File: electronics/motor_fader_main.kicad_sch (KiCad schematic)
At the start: 29 parts, among them J1 Conn_01x04_MountingPin, J2 Program, J3 Conn_01x04_MountingPin, U1 ATtiny816-M, U2 DRV8837

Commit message: updates
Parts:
- U1: value ATtiny816-M -> ATtiny1616-M; symbol MCU_Microchip_ATtiny:ATtiny816-M -> MCU_Microchip_ATtiny:ATtiny1616-M
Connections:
- net DBG_LED: now also U1.12 (PB2); no longer U1.18 (PC3)
- net TOUCH: now also U1.18 (PC3); no longer U1.8 (PA7)
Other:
- note added: "Note: Must be ATtiny1616 or ATtiny3216 for 2 independent ADC peripherals, for simultaneous touch + potentiometer."
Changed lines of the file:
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@@
 	(wire
 		(pts
+			(xy 69.85 99.06) (xy 85.09 99.06)
+		)
+		(stroke
+			(width 0)
+			(type default)
+		)
+	)
+	(wire
+		(pts
 			(xy 69.85 86.36) (xy 85.09 86.36)
 		)
@@
 		)
 	)
+	(text "Note: Must be ATtiny1616 or ATtiny3216 for\n2 independent ADC peripherals, for\nsimultaneous touch + potentiometer."
+		(exclude_from_sim no)
+		(at 28.194 50.546 0)
+		(effects
+			(font
+				(size 1.27 1.27)
+			)
+			(justify left)
+		)
+	)
 	(label "DBG_LED"
-		(at 24.13 101.6 0)
+		(at 85.09 99.06 180)
 		(effects
 			(font
 				(size 1.27 1.27)
 			)
-			(justify left bottom)
+			(justify right bottom)
 		)
 	)
@@
 	)
 	(label "TOUCH"
-		(at 85.09 88.9 180)
+		(at 24.13 101.6 0)
 		(effects
 			(font
 				(size 1.27 1.27)
 			)
-			(justify right bottom)
+			(justify left bottom)
 		)
 	)
@@
 	)
 	(symbol
-		(lib_id "MCU_Microchip_ATtiny:ATtiny816-M")
+		(lib_id "MCU_Microchip_ATtiny:ATtiny1616-M")
 		(at 54.61 88.9 0)
 		(unit 1)
@@
 		(fields_autoplaced yes)
 		(property "Reference" "U1"
-			(at 56.6294 63.5 0)
+			(at 56.8041 63.5 0)
 			(effects
 				(font
@@
 			)
 		)
-		(property "Value" "ATtiny816-M"
-			(at 56.6294 66.04 0)
+		(property "Value" "ATtiny1616-M"
+			(at 56.8041 66.04 0)
 			(effects
 				(font
@@
 			)
 		)
-		(property "Datasheet" "http://ww1.microchip.com/downloads/en/DeviceDoc/40001913A.pdf"
+		(property "Datasheet" "http://ww1.microchip.com/downloads/en/DeviceDoc/ATtiny3216_ATtiny1616-data-sheet-40001997B.pdf"
 			(at 54.61 88.9 0)
 			(effects
@@
 			)
 		)
-		(property "Description" ""
+		(property "Description" "20MHz, 16kB Flash, 2kB SRAM, 256B EEPROM, VQFN-20"
 			(at 54.61 88.9 0)
 			(effects

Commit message: Updates
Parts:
- added TP6: PA3, modified:TestPoint_THTPad_D1.0mm_Drill0.5mm_small_valuesilk, symbol Connector:TestPoint_Small
- TP1: value P?? -> PA7
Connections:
- net at TP1.1: now also U1.8 (PA7)
- net at U1.2 (PA3): now also TP6.1
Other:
- moved on the sheet: TP1
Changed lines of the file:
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@@
 	(wire
 		(pts
+			(xy 69.85 78.74) (xy 78.74 78.74)
+		)
+		(stroke
+			(width 0)
+			(type default)
+		)
+	)
+	(wire
+		(pts
 			(xy 153.67 115.57) (xy 153.67 119.38)
 		)
@@
 	(wire
 		(pts
-			(xy 69.85 88.9) (xy 85.09 88.9)
+			(xy 76.2 176.53) (xy 77.47 176.53)
 		)
 		(stroke
@@
 	(wire
 		(pts
-			(xy 76.2 176.53) (xy 77.47 176.53)
+			(xy 166.37 139.7) (xy 184.15 139.7)
 		)
 		(stroke
@@
 	(wire
 		(pts
-			(xy 166.37 139.7) (xy 184.15 139.7)
+			(xy 73.66 166.37) (xy 77.47 166.37)
 		)
 		(stroke
@@
 	(wire
 		(pts
-			(xy 73.66 166.37) (xy 77.47 166.37)
+			(xy 140.97 66.04) (xy 146.05 66.04)
 		)
 		(stroke
@@
 	(wire
 		(pts
-			(xy 140.97 66.04) (xy 146.05 66.04)
+			(xy 219.71 133.35) (xy 229.87 133.35)
 		)
 		(stroke
@@
 	(wire
 		(pts
-			(xy 219.71 133.35) (xy 229.87 133.35)
+			(xy 71.12 171.45) (xy 71.12 186.69)
 		)
 		(stroke
@@
 	(wire
 		(pts
-			(xy 71.12 171.45) (xy 71.12 186.69)
+			(xy 69.85 76.2) (xy 85.09 76.2)
 		)
 		(stroke
@@
 	(wire
 		(pts
-			(xy 69.85 76.2) (xy 85.09 76.2)
+			(xy 69.85 88.9) (xy 78.74 88.9)
 		)
 		(stroke
@@
 	(symbol
 		(lib_id "Connector:TestPoint_Small")
-		(at 90.17 60.96 0)
+		(at 78.74 88.9 0)
 		(unit 1)
 		(exclude_from_sim no)
@@
 		(dnp no)
 		(property "Reference" "TP1"
-			(at 91.44 60.96 0)
+			(at 80.01 88.9 0)
 			(effects
 				(font
@@
 			)
 		)
-		(property "Value" "P??"
-			(at 96.52 60.96 0)
+		(property "Value" "PA7"
+			(at 85.09 88.9 0)
 			(effects
 				(font
@@
 		)
 		(property "Footprint" "modified:TestPoint_THTPad_D1.0mm_Drill0.5mm_small_valuesilk"
-			(at 95.25 60.96 0)
+			(at 83.82 88.9 0)
 			(effects
 				(font
@@
 		)
 		(property "Datasheet" "~"
-			(at 95.25 60.96 0)
+			(at 83.82 88.9 0)
 			(effects
 				(font
@@
 		)
 		(property "Description" ""
-			(at 90.17 60.96 0)
+			(at 78.74 88.9 0)
 			(effects
 				(font
@@
 					(unit 1)
 				)
+			)
+		)
+	)
+	(symbol
+		(lib_id "Connector:TestPoint_Small")
+		(at 78.74 78.74 0)
+		(unit 1)
+		(exclude_from_sim no)
+		(in_bom yes)
+		(on_board yes)
+		(dnp no)
+		(property "Reference" "TP6"
+			(at 80.01 78.74 0)
+			(effects
+				(font
+					(size 1.27 1.27)
+				)
+				(justify left)
+			)
+		)
+		(property "Value" "PA3"
+			(at 85.09 78.74 0)
+			(effects
+				(font
+					(size 1.27 1.27)
+				)
+				(justify left)
+			)
+		)
+		(property "Footprint" "modified:TestPoint_THTPad_D1.0mm_Drill0.5mm_small_valuesilk"
+			(at 83.82 78.74 0)
+			(effects
+				(font
+					(size 1.27 1.27)
+				)
+				(hide yes)
+			)
+		)
+		(property "Datasheet" "~"
+			(at 83.82 78.74 0)
+			(effects
+				(font
+					(size 1.27 1.27)
+				)
+				(hide yes)
+			)
+		)
+		(property "Description" ""
+			(at 78.74 78.74 0)
+			(effects
+				(font
+					(size 1.27 1.27)
+				)
+				(hide yes)
+			)
+		)
+		(pin "1"
+		)
+		(instances
+			(project "motor_fader_main"
+				(path "/74d9b4a7-03d6-4669-9e54-5755a832b350"
+					(reference "TP6")
+					(unit 1)
+				)

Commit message: minor updates, mostly ready
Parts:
- J1: footprint Connector_PinSocket_2.54mm:PinSocket_1x05_P2.54mm_Horizontal -> modified:PinSocket_1x05_P2.54mm_Horizontal_no_silk_fill
- J3: footprint Connector_PinHeader_2.54mm:PinHeader_1x05_P2.54mm_Horizontal -> modified:PinHeader_1x05_P2.54mm_Horizontal_no_pin_silk
- JP4: value VMOT_VCC -> Vmot <-> Vio; footprint modified:SolderJumper-2_P1.3mm_Open_TrianglePad1.0x1.5mm_thermal_relief -> modified:SolderJumper-2_P1.3mm_Open_TrianglePad1.0x1.5mm_thermal_relief_labelzone
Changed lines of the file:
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@@
 			)
 		)
-		(property "Footprint" "Connector_PinHeader_2.54mm:PinHeader_1x05_P2.54mm_Horizontal"
+		(property "Footprint" "modified:PinHeader_1x05_P2.54mm_Horizontal_no_pin_silk"
 			(at 82.55 181.61 0)
 			(effects
@@
 			)
 		)
-		(property "Value" "VMOT_VCC"
+		(property "Value" "Vmot <-> Vio"
 			(at 185.42 96.52 0)
 			(effects
@@
 			)
 		)
-		(property "Footprint" "modified:SolderJumper-2_P1.3mm_Open_TrianglePad1.0x1.5mm_thermal_relief"
+		(property "Footprint" "modified:SolderJumper-2_P1.3mm_Open_TrianglePad1.0x1.5mm_thermal_relief_labelzone"
 			(at 185.42 100.33 0)
 			(effects
@@
 			)
 		)
-		(property "Footprint" "Connector_PinSocket_2.54mm:PinSocket_1x05_P2.54mm_Horizontal"
+		(property "Footprint" "modified:PinSocket_1x05_P2.54mm_Horizontal_no_silk_fill"
 			(at 82.55 166.37 0)
 			(effects

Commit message: Board cleanup, BOM cleanup
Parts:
- H1, H2, J2, JP1, JP2, JP3, JP4, TP1, TP4, TP5, TP6: now left out of the parts list
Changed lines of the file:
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@@
 		(unit 1)
 		(exclude_from_sim no)
-		(in_bom yes)
+		(in_bom no)
 		(on_board yes)
 		(dnp no)
@@
 		(unit 1)
 		(exclude_from_sim no)
-		(in_bom yes)
+		(in_bom no)
 		(on_board yes)
 		(dnp no)
@@
 		(unit 1)
 		(exclude_from_sim no)
-		(in_bom yes)
+		(in_bom no)
 		(on_board yes)
 		(dnp no)
@@
 		(unit 1)
 		(exclude_from_sim no)
-		(in_bom yes)
+		(in_bom no)
 		(on_board yes)
 		(dnp no)
@@
 		(unit 1)
 		(exclude_from_sim no)
-		(in_bom yes)
+		(in_bom no)
 		(on_board yes)
 		(dnp no)
@@
 		(unit 1)
 		(exclude_from_sim no)
-		(in_bom yes)
+		(in_bom no)
 		(on_board yes)
 		(dnp no)
@@
 		(unit 1)
 		(exclude_from_sim no)
-		(in_bom yes)
+		(in_bom no)
 		(on_board yes)
 		(dnp no)
@@
 		(unit 1)
 		(exclude_from_sim no)
-		(in_bom yes)
+		(in_bom no)
 		(on_board yes)
 		(dnp no)
@@
 		(unit 1)
 		(exclude_from_sim no)
-		(in_bom yes)
+		(in_bom no)
 		(on_board yes)
 		(dnp no)
@@
 		(unit 1)
 		(exclude_from_sim no)
-		(in_bom yes)
+		(in_bom no)
 		(on_board yes)
 		(dnp no)
@@
 		(unit 1)
 		(exclude_from_sim no)
-		(in_bom yes)
+		(in_bom no)
 		(on_board yes)
 		(dnp no)

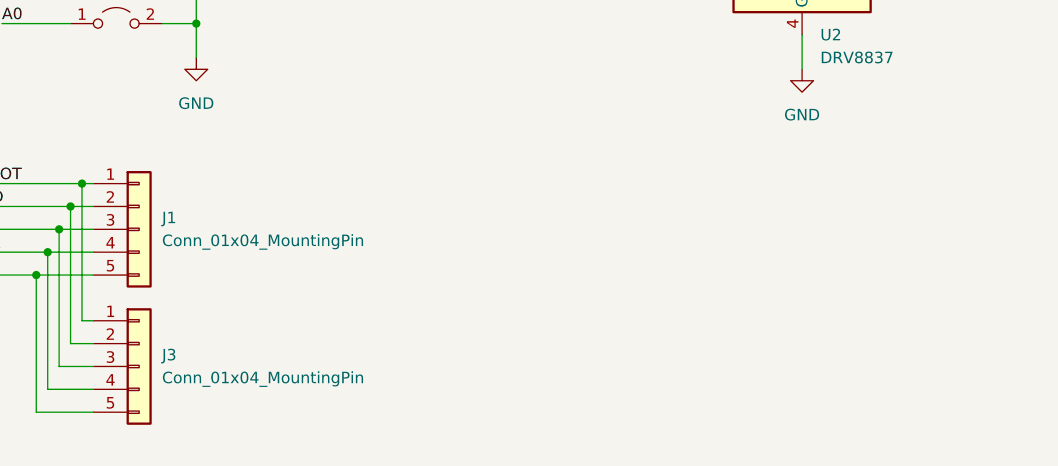
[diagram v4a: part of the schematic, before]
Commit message: Add JST SH I2C connectors
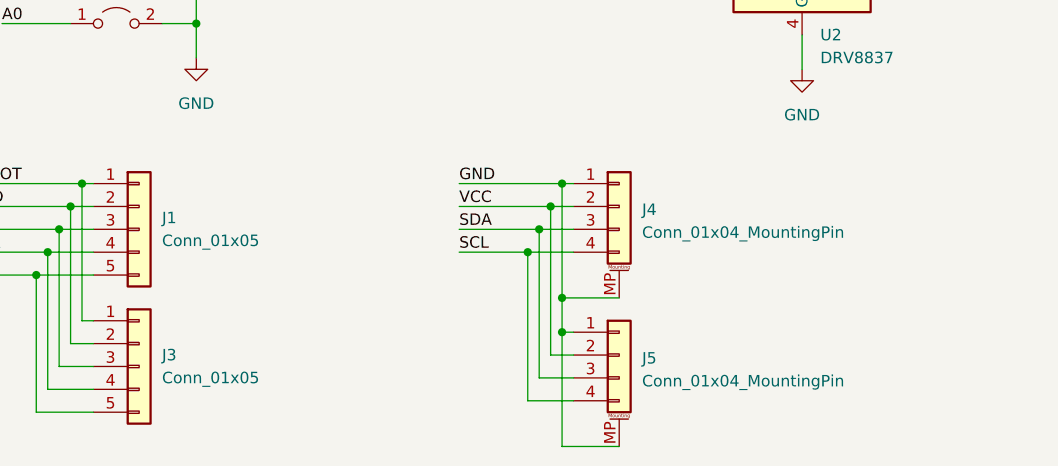
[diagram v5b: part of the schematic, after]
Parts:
- added J4, J5: Conn_01x04_MountingPin, Connector_JST:JST_SH_SM04B-SRSS-TB_1x04-1MP_P1.00mm_Horizontal, symbol Connector_Generic_MountingPin:Conn_01x04_MountingPin
- J1, J3: value Conn_01x04_MountingPin -> Conn_01x05
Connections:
- net GND: now also J4.1 (Pin_1), J4.MP (MountPin), J5.1 (Pin_1), J5.MP (MountPin)
- net SCL: now also J4.4 (Pin_4), J5.4 (Pin_4)
- net SDA: now also J4.3 (Pin_3), J5.3 (Pin_3)
- net VCC: now also J4.2 (Pin_2), J5.2 (Pin_2)

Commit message: Add JLC part number for I2C connectors
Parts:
- J4, J5: LCSC (none) -> C160404
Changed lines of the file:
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@@
+			)
+		)
+		(property "LCSC" "C160404"
+			(at 135.89 180.34 0)
+			(effects
+				(font
+					(size 1.27 1.27)
+				)
+				(hide yes)
 			)
 		)
@@
 			(at 135.89 163.83 0)
 			(effects
+				(font
+					(size 1.27 1.27)
+				)
+				(hide yes)
+			)
+		)
+		(property "LCSC" "C160404"
+			(at 135.89 163.83 0)
+			(effects

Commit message: drc
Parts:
- J4, J5: footprint Connector_JST:JST_SH_SM04B-SRSS-TB_1x04-1MP_P1.00mm_Horizontal -> modified:JST_SH_SM04B-SRSS-TB_1x04-1MP_P1.00mm_Horizontal
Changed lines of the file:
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@@
 			)
 		)
-		(property "Footprint" "Connector_JST:JST_SH_SM04B-SRSS-TB_1x04-1MP_P1.00mm_Horizontal"
+		(property "Footprint" "modified:JST_SH_SM04B-SRSS-TB_1x04-1MP_P1.00mm_Horizontal"
 			(at 135.89 180.34 0)
 			(effects
@@
 			)
 		)
-		(property "Footprint" "Connector_JST:JST_SH_SM04B-SRSS-TB_1x04-1MP_P1.00mm_Horizontal"
+		(property "Footprint" "modified:JST_SH_SM04B-SRSS-TB_1x04-1MP_P1.00mm_Horizontal"
 			(at 135.89 163.83 0)
 			(effects

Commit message: JLC part numbers
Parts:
- D1, D2: LCSC C965799 -> C2286
- J4, J5: LCSC C160404 -> C19270571
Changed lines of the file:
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@@
 			)
 		)
-		(property "LCSC" "C160404"
+		(property "LCSC" "C19270571"
 			(at 135.89 180.34 0)
 			(effects
@@
 			)
 		)
-		(property "LCSC" "C965799"
+		(property "LCSC" "C2286"
 			(at 81.28 29.21 0)
 			(effects
@@
 			)
 		)
-		(property "LCSC" "C965799"
+		(property "LCSC" "C2286"
 			(at 81.28 36.83 0)
 			(effects
@@
 			)
 		)
-		(property "LCSC" "C160404"
+		(property "LCSC" "C19270571"
 			(at 135.89 163.83 0)
 			(effects
